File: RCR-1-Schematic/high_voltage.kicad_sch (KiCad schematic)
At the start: 29 parts, among them J2 BNC

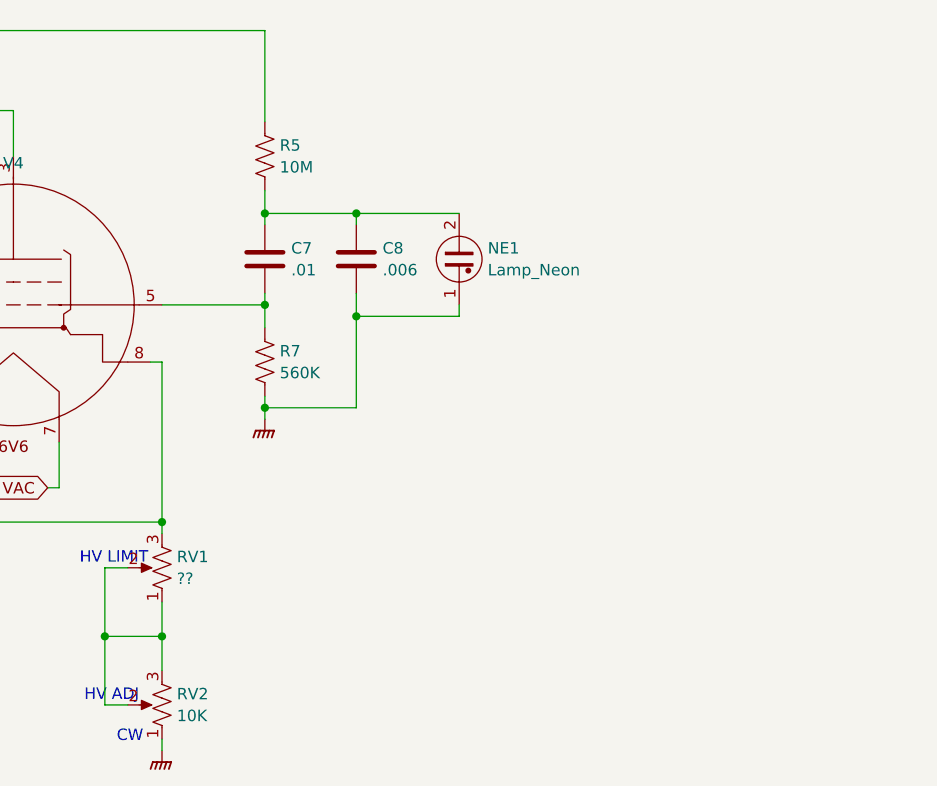
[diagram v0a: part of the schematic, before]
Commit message: Add some oscilloscope screenshots, fixed some mistakes
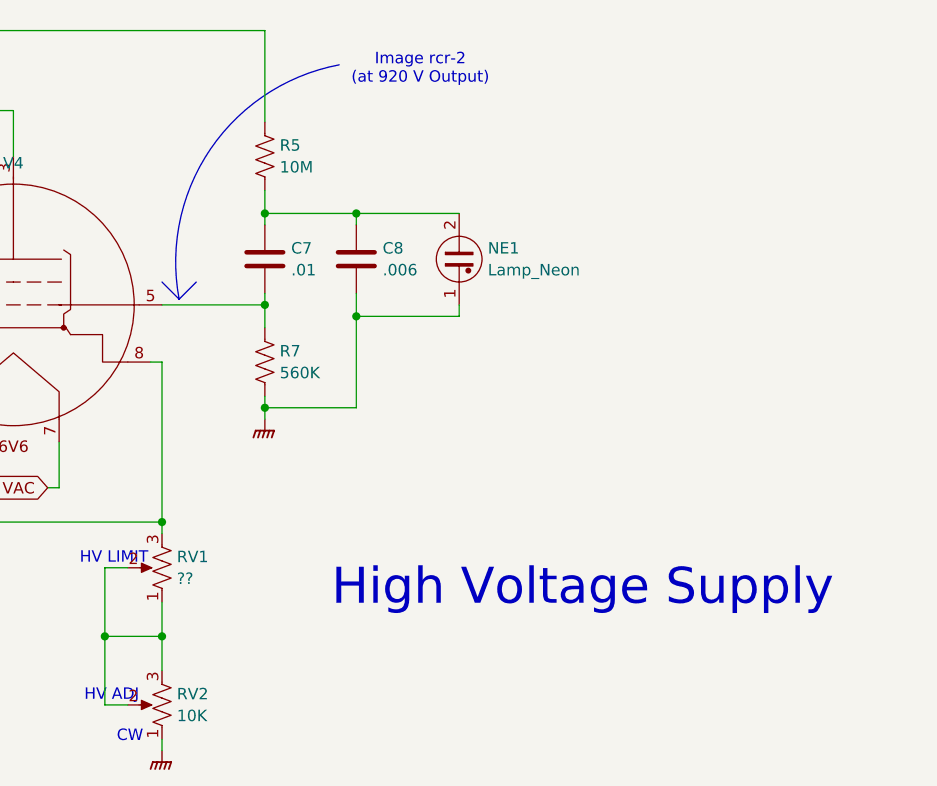
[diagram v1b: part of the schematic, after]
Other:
- note added: "High Voltage Supply"
- note added: "Image rcr-2 (at 920 V Output)"
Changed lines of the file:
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@@
 		(comment 1 "Schematic by Steve Conklin")
 	)
+	(arc
+		(start 114.935 60.325)
+		(mid 118.433 43.6251)
+		(end 132.715 34.29)
+		(stroke
+			(width 0)
+			(type default)
+		)
+		(fill
+			(type none)
+		)
+	)
 	(text " To Geiger–Müller tube"
 		(exclude_from_sim no)
@@
 		)
 	)
+	(text "High Voltage Supply"
+		(exclude_from_sim no)
+		(at 159.766 92.456 0)
+		(effects
+			(font
+				(size 4 4)
+			)
+		)
+	)
+	(text "Image rcr-2\n(at 920 V Output)"
+		(exclude_from_sim no)
+		(at 141.732 34.798 0)
+		(effects
+			(font
+				(size 1.27 1.27)
+			)
+		)
+	)
 	(text "CW"
 		(exclude_from_sim no)
@@
 		)
 		(stroke
+			(width 0)
+			(type default)
+		)
+	)
+	(polyline
+		(pts
+			(xy 114.935 60.325) (xy 116.84 58.42)
+		)
+		(stroke
+			(width 0)
+			(type default)
+		)
+	)
+	(polyline
+		(pts
+			(xy 113.03 58.42) (xy 114.935 60.325)
+		)
+		(stroke

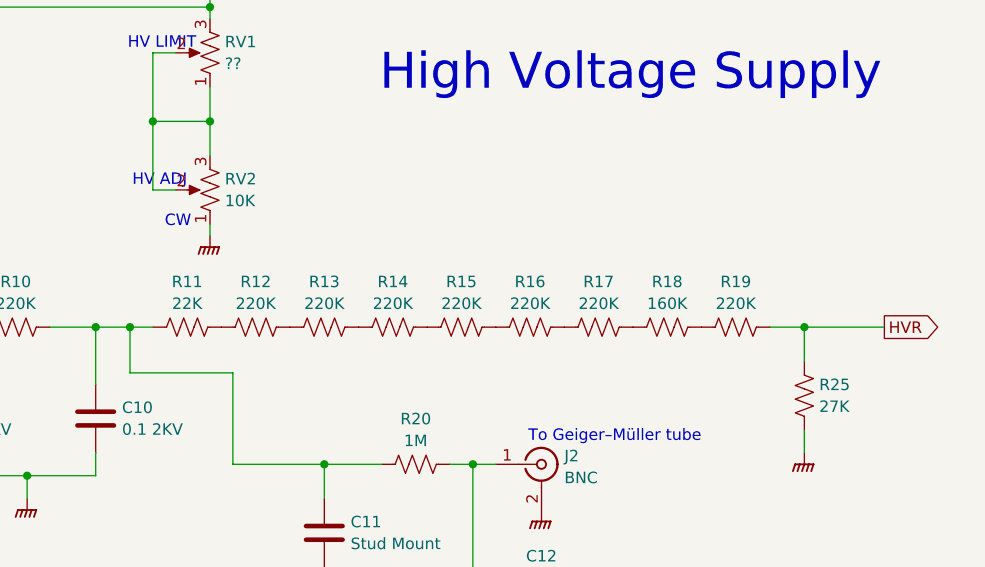
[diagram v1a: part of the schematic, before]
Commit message: Update schematic and README to reflect changes/updates
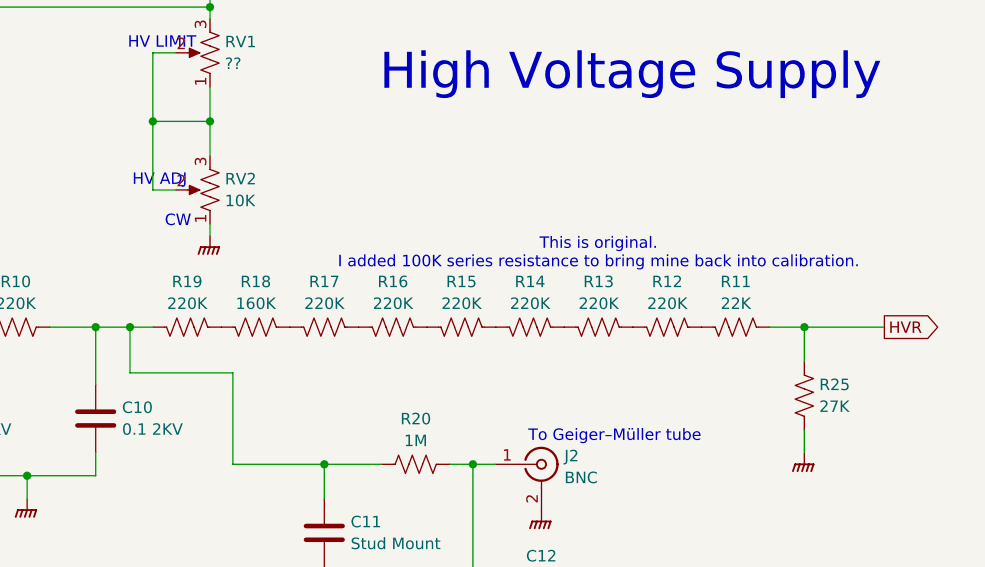
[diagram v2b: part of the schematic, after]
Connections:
- net HVR: now also R11.1; no longer R19.2
- net at C10.1, C11.1, R10.2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: now also R19.2; no longer R11.1
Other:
- note added: "This is original. I added 100K series resistance to bring mine back into calibration."
- moved on the sheet: R11, R12, R13, R14, R15, R16, R17, R18, R19
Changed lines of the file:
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@@
 		)
 	)
+	(text "This is original.\nI added 100K series resistance to bring mine back into calibration."
+		(exclude_from_sim no)
+		(at 156.21 112.522 0)
+		(effects
+			(font
+				(size 1.27 1.27)
+			)
+		)
+	)
 	(junction
 		(at 100.33 120.65)
@@
 	)
 	(junction
-		(at 179.07 120.65)
+		(at 113.03 85.09)
 		(diameter 0)
 		(color 0 0 0 0)
 	)
 	(junction
-		(at 113.03 85.09)
+		(at 179.07 120.65)
 		(diameter 0)
 		(color 0 0 0 0)
@@
 	(wire
 		(pts
+			(xy 175.26 120.65) (xy 179.07 120.65)
+		)
+		(stroke
+			(width 0)
+			(type default)
+		)
+	)
+	(wire
+		(pts
 			(xy 139.7 135.89) (xy 142.24 135.89)
 		)
@@
 	(wire
 		(pts
-			(xy 179.07 120.65) (xy 175.26 120.65)
-		)
-		(stroke
-			(width 0)
-			(type default)
-		)
-	)
-	(wire
-		(pts
 			(xy 101.6 81.28) (xy 100.33 81.28)
 		)
@@
 	(symbol
 		(lib_id "Device:R_US")
-		(at 156.21 120.65 90)
+		(at 125.73 120.65 270)
+		(mirror x)
 		(unit 1)
 		(exclude_from_sim no)
@@
 		(fields_autoplaced yes)
 		(property "Reference" "R17"
-			(at 156.21 115.6165 90)
+			(at 125.73 115.6165 90)
 			(effects
 				(font
@@
 		)
 		(property "Value" "220K"
-			(at 156.21 118.0408 90)
+			(at 125.73 118.0408 90)
 			(effects
 				(font
@@
 		)
 		(property "Footprint" ""
-			(at 156.464 119.634 90)
+			(at 125.476 119.634 90)
 			(effects
 				(font
@@
 		)
 		(property "Datasheet" "~"
-			(at 156.21 120.65 0)
+			(at 125.73 120.65 0)
 			(effects
 				(font
@@
 		)
 		(property "Description" "Resistor, US symbol"
-			(at 156.21 120.65 0)
+			(at 125.73 120.65 0)
 			(effects
 				(font
@@
 	(symbol
 		(lib_id "Device:R_US")
-		(at 163.83 120.65 90)
+		(at 118.11 120.65 270)
+		(mirror x)
 		(unit 1)
 		(exclude_from_sim no)
@@
 		(fields_autoplaced yes)
 		(property "Reference" "R18"
-			(at 163.83 115.6165 90)
+			(at 118.11 115.6165 90)
 			(effects
 				(font
@@
 		)
 		(property "Value" "160K"
-			(at 163.83 118.0408 90)
+			(at 118.11 118.0408 90)
 			(effects
 				(font
@@
 		)
 		(property "Footprint" ""
-			(at 164.084 119.634 90)
+			(at 117.856 119.634 90)
 			(effects
 				(font
@@
 		)
 		(property "Datasheet" "~"
-			(at 163.83 120.65 0)
+			(at 118.11 120.65 0)
 			(effects
 				(font
@@
 		)
 		(property "Description" "Resistor, US symbol"
-			(at 163.83 120.65 0)
+			(at 118.11 120.65 0)
 			(effects
 				(font
@@
 	(symbol
 		(lib_id "Device:R_US")
-		(at 148.59 120.65 90)
+		(at 133.35 120.65 270)
+		(mirror x)
 		(unit 1)
 		(exclude_from_sim no)
@@
 		(fields_autoplaced yes)
 		(property "Reference" "R16"
-			(at 148.59 115.6165 90)
+			(at 133.35 115.6165 90)
 			(effects
 				(font
@@
 		)
 		(property "Value" "220K"
-			(at 148.59 118.0408 90)
+			(at 133.35 118.0408 90)
 			(effects
 				(font
@@
 		)
 		(property "Footprint" ""
-			(at 148.844 119.634 90)
+			(at 133.096 119.634 90)
 			(effects
 				(font
@@
 		)
 		(property "Datasheet" "~"
-			(at 148.59 120.65 0)
+			(at 133.35 120.65 0)
 			(effects
 				(font
@@
 		)
 		(property "Description" "Resistor, US symbol"
-			(at 148.59 120.65 0)
+			(at 133.35 120.65 0)
 			(effects
 				(font
@@
 	(symbol
 		(lib_id "Device:R_US")
-		(at 110.49 120.65 90)
+		(at 171.45 120.65 270)
+		(mirror x)
 		(unit 1)
 		(exclude_from_sim no)
@@
 		(fields_autoplaced yes)
 		(property "Reference" "R11"
-			(at 110.49 115.6165 90)
+			(at 171.45 115.6165 90)
 			(effects
 				(font
@@
 		)
 		(property "Value" "22K"
-			(at 110.49 118.0408 90)
+			(at 171.45 118.0408 90)
 			(effects
 				(font
@@
 		)
 		(property "Footprint" ""
-			(at 110.744 119.634 90)
+			(at 171.196 119.634 90)
 			(effects
 				(font
@@
 		)
 		(property "Datasheet" "~"
-			(at 110.49 120.65 0)
+			(at 171.45 120.65 0)
 			(effects
 				(font
@@
 		)
 		(property "Description" "Resistor, US symbol"
-			(at 110.49 120.65 0)
+			(at 171.45 120.65 0)
 			(effects
 				(font
@@
 	(symbol
 		(lib_id "Device:R_US")
-		(at 125.73 120.65 90)
+		(at 156.21 120.65 270)
+		(mirror x)
 		(unit 1)
 		(exclude_from_sim no)
@@
 		(fields_autoplaced yes)
 		(property "Reference" "R13"
-			(at 125.73 115.6165 90)
+			(at 156.21 115.6165 90)
 			(effects
 				(font
@@
 		)
 		(property "Value" "220K"
-			(at 125.73 118.0408 90)
+			(at 156.21 118.0408 90)
 			(effects
 				(font
@@
 		)
 		(property "Footprint" ""
-			(at 125.984 119.634 90)
+			(at 155.956 119.634 90)
 			(effects
 				(font
@@
 		)
 		(property "Datasheet" "~"
-			(at 125.73 120.65 0)
+			(at 156.21 120.65 0)
 			(effects
 				(font
@@
 		)
 		(property "Description" "Resistor, US symbol"
-			(at 125.73 120.65 0)
+			(at 156.21 120.65 0)
 			(effects
 				(font
@@
 	(symbol
 		(lib_id "Device:R_US")
-		(at 140.97 120.65 90)
+		(at 140.97 120.65 270)
+		(mirror x)
 		(unit 1)
 		(exclude_from_sim no)
@@
 		)
 		(property "Footprint" ""
-			(at 141.224 119.634 90)
+			(at 140.716 119.634 90)
 			(effects
 				(font
@@
 	(symbol
 		(lib_id "Device:R_US")
-		(at 171.45 120.65 90)
+		(at 110.49 120.65 270)
+		(mirror x)
 		(unit 1)
 		(exclude_from_sim no)
@@
 		(fields_autoplaced yes)
 		(property "Reference" "R19"
-			(at 171.45 115.6165 90)
+			(at 110.49 115.6165 90)
 			(effects
 				(font
@@
 		)
 		(property "Value" "220K"
-			(at 171.45 118.0408 90)
+			(at 110.49 118.0408 90)
 			(effects
 				(font
@@
 		)
 		(property "Footprint" ""
-			(at 171.704 119.634 90)
+			(at 110.236 119.634 90)
 			(effects
 				(font
@@
 		)
 		(property "Datasheet" "~"
-			(at 171.45 120.65 0)
+			(at 110.49 120.65 0)
 			(effects
 				(font
@@
 		)
 		(property "Description" "Resistor, US symbol"
-			(at 171.45 120.65 0)
+			(at 110.49 120.65 0)
 			(effects
 				(font
@@
 	(symbol
 		(lib_id "Device:R_US")
-		(at 118.11 120.65 90)
+		(at 163.83 120.65 270)
+		(mirror x)
 		(unit 1)
 		(exclude_from_sim no)
@@
 		(fields_autoplaced yes)
 		(property "Reference" "R12"
-			(at 118.11 115.6165 90)
+			(at 163.83 115.6165 90)
 			(effects
 				(font
@@
 		)
 		(property "Value" "220K"
-			(at 118.11 118.0408 90)
+			(at 163.83 118.0408 90)
 			(effects
 				(font
@@
 		)
 		(property "Footprint" ""
-			(at 118.364 119.634 90)
+			(at 163.576 119.634 90)
 			(effects
 				(font
@@
 		)
 		(property "Datasheet" "~"
-			(at 118.11 120.65 0)
+			(at 163.83 120.65 0)
 			(effects
 				(font
@@
 		)
 		(property "Description" "Resistor, US symbol"
-			(at 118.11 120.65 0)
+			(at 163.83 120.65 0)
 			(effects
 				(font
@@
 	(symbol
 		(lib_id "Device:R_US")
-		(at 133.35 120.65 90)
+		(at 148.59 120.65 270)
+		(mirror x)
 		(unit 1)
 		(exclude_from_sim no)
@@
 		(fields_autoplaced yes)
 		(property "Reference" "R14"
-			(at 133.35 115.6165 90)
+			(at 148.59 115.6165 90)
 			(effects
 				(font
@@
 		)
 		(property "Value" "220K"
-			(at 133.35 118.0408 90)
+			(at 148.59 118.0408 90)
 			(effects
 				(font
@@
 		)
 		(property "Footprint" ""
-			(at 133.604 119.634 90)
+			(at 148.336 119.634 90)
 			(effects
 				(font
@@
 		)
 		(property "Datasheet" "~"
-			(at 133.35 120.65 0)
+			(at 148.59 120.65 0)
 			(effects
 				(font
@@
 		)
 		(property "Description" "Resistor, US symbol"
-			(at 133.35 120.65 0)
+			(at 148.59 120.65 0)
 			(effects
 				(font
